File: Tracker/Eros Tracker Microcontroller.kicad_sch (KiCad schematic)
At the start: 15 parts, among them M1 Motor_DC, Q1 BSS138, Q5 CJ2305, SW2 SW_DPST, U1 ESP32-C3-WROOM-02-N4

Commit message: Midway through board layout
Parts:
- removed Q1 (x3): BSS138, Package_TO_SOT_SMD:SOT-23, symbol Transistor_FET:BSS138
- removed Q5: CJ2305, Package_TO_SOT_SMD:SOT-23, symbol Transistor_FET:AO3401A
- removed R14: 100k, symbol Device:R_US
- removed R15: 10k, symbol Device:R_US
- removed SW2: SW_DPST, symbol Switch:SW_DPST
- added D1: BAT54C, Package_TO_SOT_SMD:SOT-23, symbol Diode:BAT54C
- added LED1, LED2: APDA3020LVBC_D, Eros Tracker:APDA3020LVBCD, symbol Eros Tracker:APDA3020LVBC_D
- added Q1, Q2: NX138BKSX, Eros Tracker:SOT65P210X110-6N, symbol Eros Tracker:NX138BKSX
- added Q3: DMP31D7LDW-7, Eros Tracker:SOT65P210X110-6N, symbol Eros Tracker:DMP31D7LDW-7
- added R11, R15: 10k 1%, Resistor_SMD:R_0805_2012Metric, symbol Device:R_US
- added R11: 45k3 1%, Resistor_SMD:R_0805_2012Metric, symbol Device:R_US
- added R15 (x2): 22R, Resistor_SMD:R_0805_2012Metric, symbol Device:R_US
- added SW1: EVQ-P7A01P, Eros Tracker:EVQ-9P701P, symbol Eros Tracker:EVQ-P7A01P
- C4: footprint (none) -> Capacitor_SMD:C_0805_2012Metric; Manufacturer_Name (none) -> Samsung; Manufacturer_Part_Number (none) -> CL21B104MACNNNC; Mouser Part Number (none) -> 187-CL21B104MACNNNC; Mouser Price/Stock (none) -> https://www.mouser.com/ProductDetail/Samsung-Electro-Mechan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
- JP1, M1: footprint (none) -> Jumper:SolderJumper-2_P1.3mm_Open_RoundedPad1.0x1.5mm
- R11: footprint (none) -> Resistor_SMD:R_0805_2012Metric; Manufacturer_Name (none) -> YAGEO; Manufacturer_Part_Number (none) -> RT0805FRE132K2L; Mouser Part Number (none) -> 603-RT0805FRE132K2L; Mouser Price/Stock (none) -> https://www.mouser.com/ProductDetail/YAGEO/RT0805FRE132K2L?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
- R13, R9: footprint (none) -> Resistor_SMD:R_0805_2012Metric; Manufacturer_Name (none) -> YAGEO; Manufacturer_Part_Number (none) -> RT0805FRE07100KL; Mouser Part Number (none) -> 603-RT0805FRE07100KL; Mouser Price/Stock (none) -> https://www.mouser.com/ProductDetail/YAGEO/RT0805FRE07100KL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
- U1: footprint Eros Tracker:MODULE_ESP32-C3-WROOM-02-H4 -> Eros Tracker:ESP32-C3-WROOM-02-N4-MODULE_ESP32-C3-WROOM-02-H4; Manufacturer_Name (none) -> Espressif Systems; Manufacturer_Part_Number (none) -> ESP32-C3-WROOM-02-N4; Mouser Part Number (none) -> 356-ESP32C3WROOM02N4; Mouser Price/Stock (none) -> https://www.mouser.com/ProductDetail/Espressif-Systems/ESP3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
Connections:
- net +3.3V is gone; now on net +3V3: C4.1
- net +3V3: now also Q2.3 (D2), Q3.3 (D2), Q3.6 (D1), SW1.3 (COM_1), SW1.4 (COM_2)
- net +BATT: now also D1.3, R11.1
- net ENABLE: now also Q3.1 (S1)
- net GND: now also Q1.1 (S1), Q1.4 (S2), Q2.1 (S1), R11.2, R15.2, R15.2, R15.2
- net TACT_MOTOR0: now also Q1.5 (G2)
- net TACT_MOTOR1: now also Q1.2 (G1)
- net ~{BUTTON_INPUT}: now also Q2.5 (G2), R15.1, SW1.1 (NO_1), SW1.2 (NO_2)
- net at R13.2: now also Q2.2 (G1), Q2.4 (S2)
- net ~{BAT_STAT_CHARGING}: now reaches R9.2
- net ~{BAT_STAT_CHARGING}: now also Q2.6 (D1), Q3.2 (G1)
- net at M1.2 (-): now also D1.2, Q1.3 (D2)
- net LED renamed ~{LED}
- net ~{LED}: now also Q3.5 (G2)
- net VBATT_MON: no longer names the net of U1.17 (IO1)
- net VBATT_MON: now also R11.1, R11.2
- new net: LED1.2 (A), LED2.2 (A), Q3.4 (S2)
- new net: LED1.1 (K), R15.1
- new net: LED2.1 (K), R15.1
- new net -EXT_MOTOR: D1.1, Q1.6 (D1)
- no-connect marks 0 -> 2
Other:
- moved on the sheet: C4, JP1, R11, U1

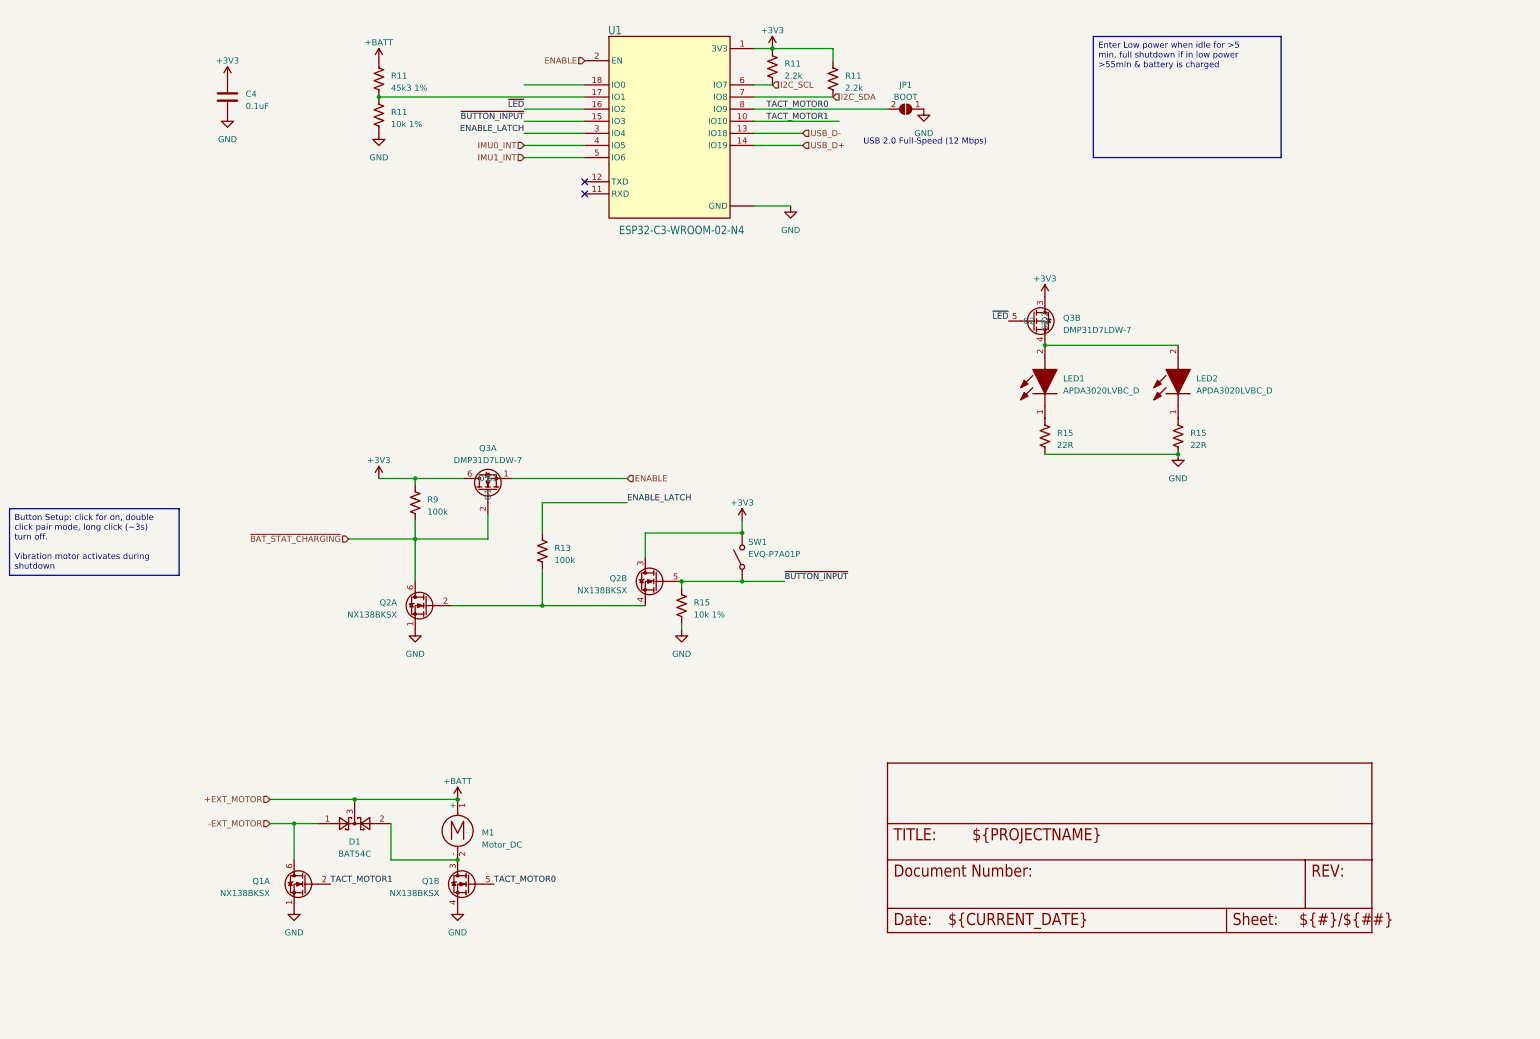
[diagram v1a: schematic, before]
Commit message: Added cuts and jumps for Rev A
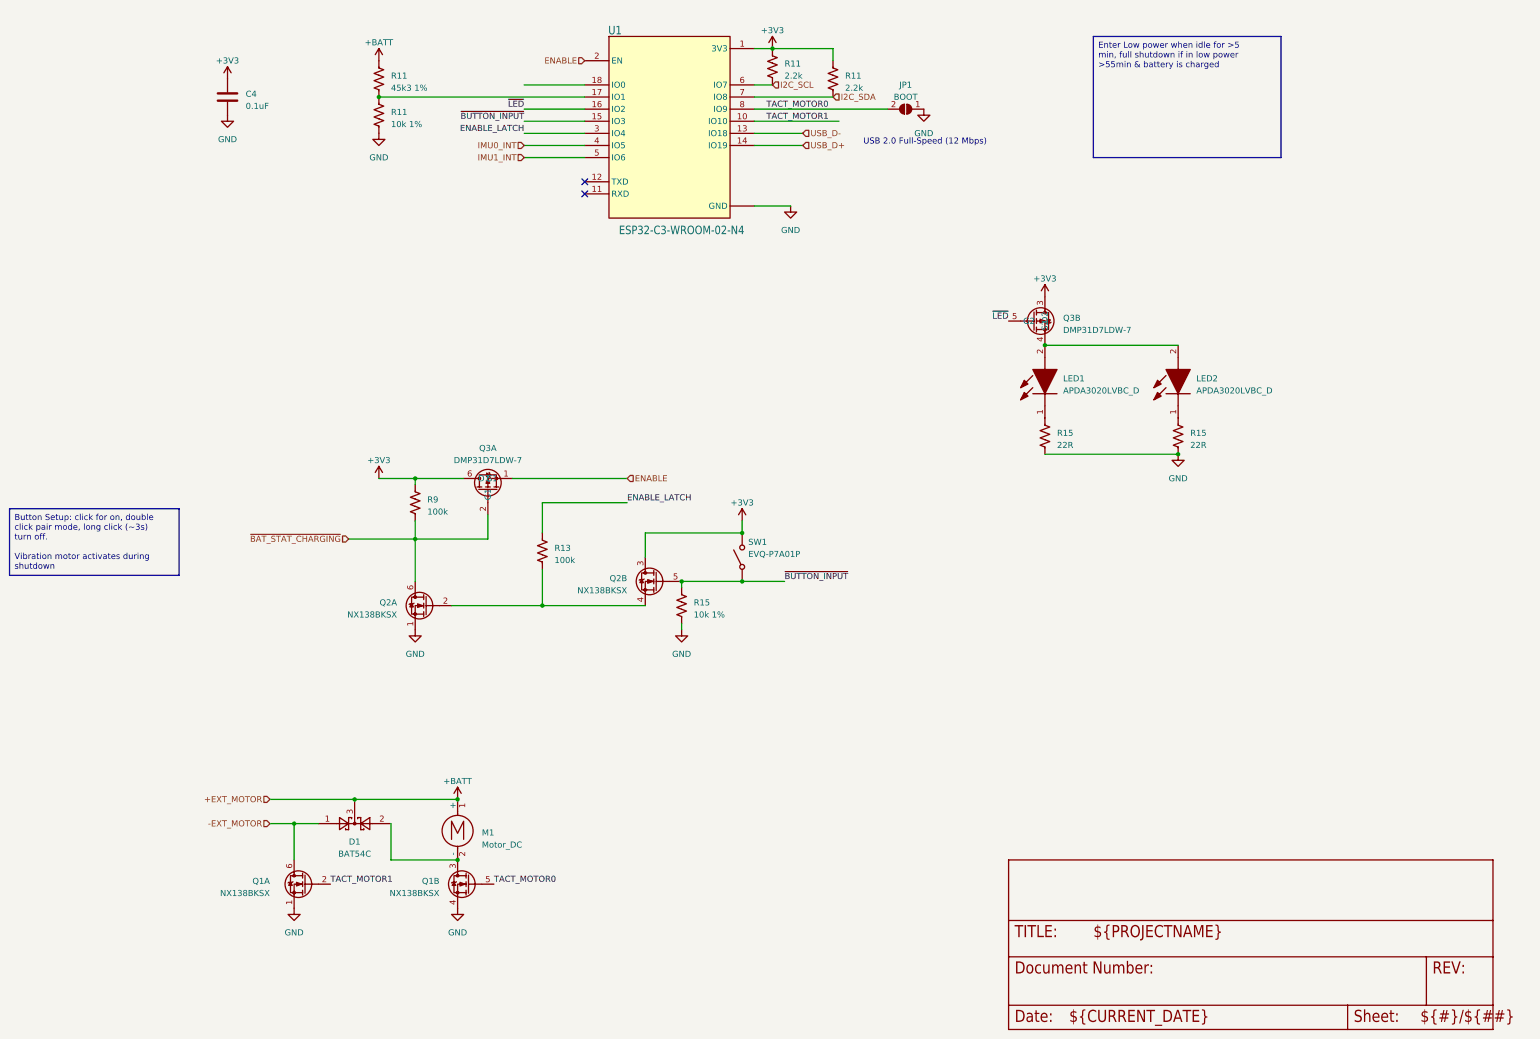
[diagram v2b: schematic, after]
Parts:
- JP1: now left out of the parts list
- LED1, LED2: footprint Eros Tracker:APDA3020LVBCD -> APDA3020LVBCD
- Q3: footprint Eros Tracker:SOT65P210X110-6N -> SOT65P210X110-6N
- SW1: footprint Eros Tracker:EVQ-9P701P -> EVQP7J01P
- U1: footprint Eros Tracker:ESP32-C3-WROOM-02-N4-MODULE_ESP32-C3-WROOM-02-H4 -> Eros Tracker:MODULE_ESP32-C3-WROOM-02-H4
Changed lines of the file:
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@@
       (effects (font (size 1.27 1.27)) hide)
     )
-    (property "Datasheet" "https://www.mouser.com/datasheet/2/447/PYu_RT_1_to_0_01_RoHS_L_12-3003070.pdf" (at 118.11 153.67 0)
+    (property "Datasheet" "~" (at 118.11 153.67 0)
       (effects (font (size 1.27 1.27)) hide)
     )
@@
       (effects (font (size 1.27 1.27)) hide)
     )
-    (property "Datasheet" "https://www.mouser.com/datasheet/2/447/PYu_RT_1_to_0_01_RoHS_L_12-3003070.pdf" (at 179.07 54.61 0)
+    (property "Datasheet" "~" (at 179.07 54.61 0)
       (effects (font (size 1.27 1.27)) hide)
     )
@@
       (effects (font (size 1.27 1.27)) hide)
     )
-    (property "Datasheet" "https://www.mouser.com/datasheet/2/585/MLCC-1837944.pdf" (at 52.07 58.42 0)
+    (property "Datasheet" "~" (at 52.07 58.42 0)
       (effects (font (size 1.27 1.27)) hide)
     )
@@
   )
   (symbol (lib_id "Jumper:SolderJumper_2_Open") (at 194.31 60.96 180) (unit 1)
-    (in_bom yes) (on_board yes) (dnp no) (fields_autoplaced)
+    (in_bom no) (on_board yes) (dnp no) (fields_autoplaced)
     (property "Reference" "JP1" (at 194.31 55.88 0)
       (effects (font (size 1.27 1.27)))
@@
       (effects (font (size 1.27 1.27)) hide)
     )
-    (property "Datasheet" "https://www.amazon.com/SQXBK-Vibrating-Vibration-Mobile-10x2-7mm/dp/B0B2CZ36FC/ref=rvi_sccl_6/132-6042082-3290345?pd_rd_w=i4BcR&content-id=amzn1.sym.f5690a4d-f2bb-45d9-9d1b-736fee412437&pf_rd_p=f5690a4d-f2bb-45d9-9d1b-736fee412437&pf_rd_r=J8FKV4CPMB9CFE4TY7QZ&pd_rd_wg=d6x4K&pd_rd_r=55f34269-bb47-489b-868d-2c3abb9572e5&pd_rd_i=B0B2CZ36FC&th=1" (at 100.33 213.106 0)
+    (property "Datasheet" "~" (at 100.33 213.106 0)
       (effects (font (size 1.27 1.27)) hide)
     )
@@
       (effects (font (size 1.27 1.27)))
     )
-    (property "Footprint" "Eros Tracker:SOT65P210X110-6N" (at 201.6 119.38 0)
+    (property "Footprint" "SOT65P210X110-6N" (at 201.6 119.38 0)
       (effects (font (size 1.27 1.27)) (justify left top) hide)
     )
@@
       (effects (font (size 1.27 1.27)) (justify left))
     )
-    (property "Footprint" "Eros Tracker:SOT65P210X110-6N" (at 242.57 200.33 0)
+    (property "Footprint" "SOT65P210X110-6N" (at 242.57 200.33 0)
       (effects (font (size 1.27 1.27)) (justify left top) hide)
     )
@@
       (effects (font (size 1.27 1.27)) hide)
     )
-    (property "Datasheet" "https://www.mouser.com/datasheet/2/447/PYu_RT_1_to_0_01_RoHS_L_12-3003070.pdf" (at 83.82 62.23 0)
+    (property "Datasheet" "~" (at 83.82 62.23 0)
       (effects (font (size 1.27 1.27)) hide)
     )
@@
       (effects (font (size 1.27 1.27)) hide)
     )
-    (property "Datasheet" "https://www.mouser.com/datasheet/2/447/PYu_RT_1_to_0_01_RoHS_L_12-3003070.pdf" (at 166.37 52.07 0)
+    (property "Datasheet" "~" (at 166.37 52.07 0)
       (effects (font (size 1.27 1.27)) hide)
     )
@@
     )
   )
-  (symbol (lib_id "Eros Tracker-eagle-import:FRAME_A_L") (at 190.5 233.68 0) (unit 2)
+  (symbol (lib_id "Eros Tracker-eagle-import:FRAME_A_L") (at 215.9 254 0) (unit 2)
     (in_bom yes) (on_board yes) (dnp no)
-    (property "Reference" "#FRAME1" (at 190.5 233.68 0)
-      (effects (font (size 1.27 1.27)) hide)
-    )
-    (property "Value" "FRAME_A_L" (at 190.5 233.68 0)
-      (effects (font (size 1.27 1.27)) hide)
-    )
-    (property "Footprint" "" (at 190.5 233.68 0)
-      (effects (font (size 1.27 1.27)) hide)
-    )
-    (property "Datasheet" "" (at 190.5 233.68 0)
+    (property "Reference" "#FRAME1" (at 215.9 254 0)
+      (effects (font (size 1.27 1.27)) hide)
+    )
+    (property "Value" "FRAME_A_L" (at 215.9 254 0)
+      (effects (font (size 1.27 1.27)) hide)
+    )
+    (property "Footprint" "" (at 215.9 254 0)
+      (effects (font (size 1.27 1.27)) hide)
+    )
+    (property "Datasheet" "" (at 215.9 254 0)
       (effects (font (size 1.27 1.27)) hide)
     )
@@
       (effects (font (size 1.27 1.27)) hide)
     )
-    (property "Datasheet" "https://www.mouser.com/datasheet/2/447/PYu_RT_1_to_0_01_RoHS_L_12-3003070.pdf" (at 223.52 129.54 0)
+    (property "Datasheet" "~" (at 223.52 129.54 0)
       (effects (font (size 1.27 1.27)) hide)
     )
@@
       (effects (font (size 1.27 1.27)) hide)
     )
-    (property "Datasheet" "https://www.mouser.com/datasheet/2/447/PYu_RT_1_to_0_01_RoHS_L_12-3003070.pdf" (at 91.44 143.51 0)
+    (property "Datasheet" "~" (at 91.44 143.51 0)
       (effects (font (size 1.27 1.27)) hide)
     )
@@
       (effects (font (size 1.27 1.27)) hide)
     )
-    (property "Datasheet" "https://www.mouser.com/datasheet/2/447/PYu_RT_1_to_0_01_RoHS_L_12-3003070.pdf" (at 83.82 54.61 0)
+    (property "Datasheet" "~" (at 83.82 54.61 0)
       (effects (font (size 1.27 1.27)) hide)
     )
@@
       (effects (font (size 1.27 1.27)) hide)
     )
-    (property "Datasheet" "https://www.mouser.com/datasheet/2/447/PYu_RT_1_to_0_01_RoHS_L_12-3003070.pdf" (at 251.46 129.54 0)
+    (property "Datasheet" "~" (at 251.46 129.54 0)
       (effects (font (size 1.27 1.27)) hide)
     )
@@
       (effects (font (size 1.27 1.27)) hide)
     )
-    (property "Datasheet" "https://www.mouser.com/datasheet/2/447/PYu_RT_1_to_0_01_RoHS_L_12-3003070.pdf" (at 147.32 165.1 0)
+    (property "Datasheet" "~" (at 147.32 165.1 0)
       (effects (font (size 1.27 1.27)) hide)
     )
@@
       (effects (font (size 1.27 1.27)) (justify right))
     )
-    (property "Footprint" "Eros Tracker:APDA3020LVBCD" (at 345.11 113.03 0)
+    (property "Footprint" "APDA3020LVBCD" (at 345.11 113.03 0)
       (effects (font (size 1.27 1.27)) (justify left bottom) hide)
     )
@@
       (effects (font (size 1.778 1.5113)))
     )
-    (property "Footprint" "Eros Tracker:ESP32-C3-WROOM-02-N4-MODULE_ESP32-C3-WROOM-02-H4" (at 153.67 87.63 0)
+    (property "Footprint" "Eros Tracker:MODULE_ESP32-C3-WROOM-02-H4" (at 153.67 87.63 0)
       (effects (font (size 1.27 1.27)) hide)
     )
@@
       (effects (font (size 1.27 1.27)) (justify right))
     )
-    (property "Footprint" "Eros Tracker:APDA3020LVBCD" (at 317.17 113.03 0)
+    (property "Footprint" "APDA3020LVBCD" (at 317.17 113.03 0)
       (effects (font (size 1.27 1.27)) (justify left bottom) hide)
     )
@@
       (effects (font (size 1.27 1.27)) (justify right))
     )
-    (property "Footprint" "Eros Tracker:EVQ-9P701P" (at 254.94 133.35 0)
-      (effects (font (size 1.27 1.27)) (justify left top) hide)
-    )
+    (property "Footprint" "EVQP7J01P" (at 254.94 133.35 0)
+      (effects (font (size 1.27 1.27)) (justify left top) hide)
+    )
